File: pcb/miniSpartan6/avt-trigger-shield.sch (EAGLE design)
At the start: 20 parts

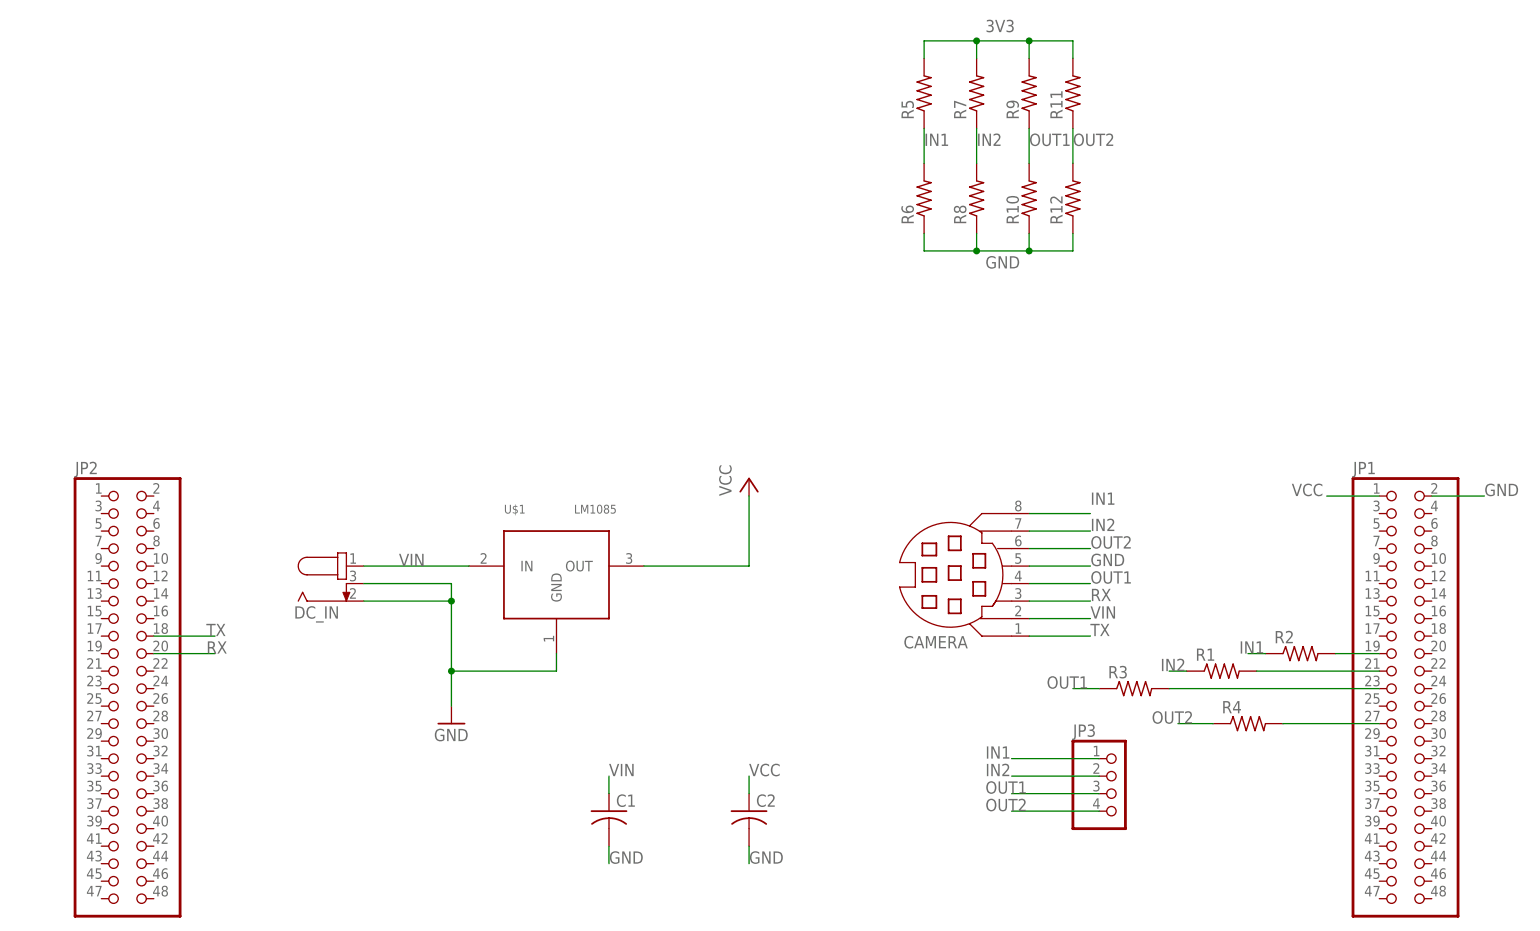
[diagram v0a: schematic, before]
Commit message: finished avt trigger board
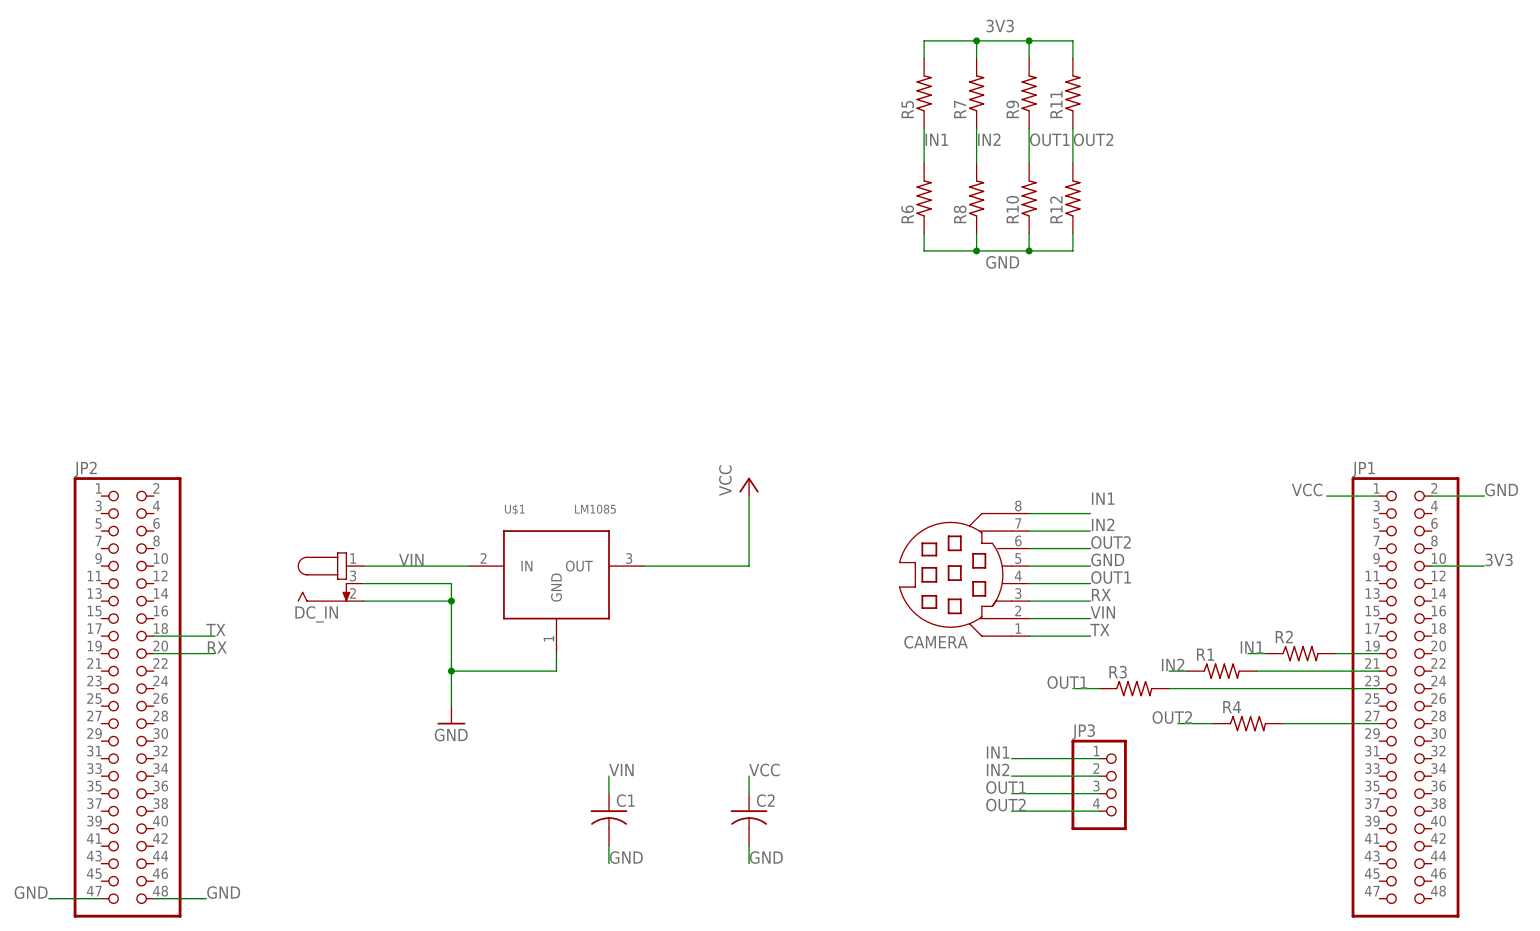
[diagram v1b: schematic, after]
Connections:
- net 3V3: now also JP1.10
- net GND: now also JP2.47, JP2.48
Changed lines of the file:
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@@
 <wire x1="142.24" y1="115.57" x2="142.24" y2="118.11" width="0.1524" layer="91"/>
+</segment>
+<segment>
+<pinref part="JP2" gate="A" pin="47"/>
+<wire x1="1.27" y1="21.59" x2="-6.35" y2="21.59" width="0.1524" layer="91"/>
+<label x="-11.43" y="21.59" size="1.778" layer="95"/>
+</segment>
+<segment>
+<pinref part="JP2" gate="A" pin="48"/>
+<wire x1="8.89" y1="21.59" x2="16.51" y2="21.59" width="0.1524" layer="91"/>
+<label x="16.51" y="21.59" size="1.778" layer="95"/>
 </segment>
 </net>
@@
 <label x="129.54" y="147.32" size="1.778" layer="95"/>
 </segment>
+<segment>
+<pinref part="JP1" gate="A" pin="10"/>
+<wire x1="194.31" y1="69.85" x2="201.93" y2="69.85" width="0.1524" layer="91"/>
+<label x="201.93" y="69.85" size="1.778" layer="95"/>
+</segment>
 </net>

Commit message: fixed pin assignments
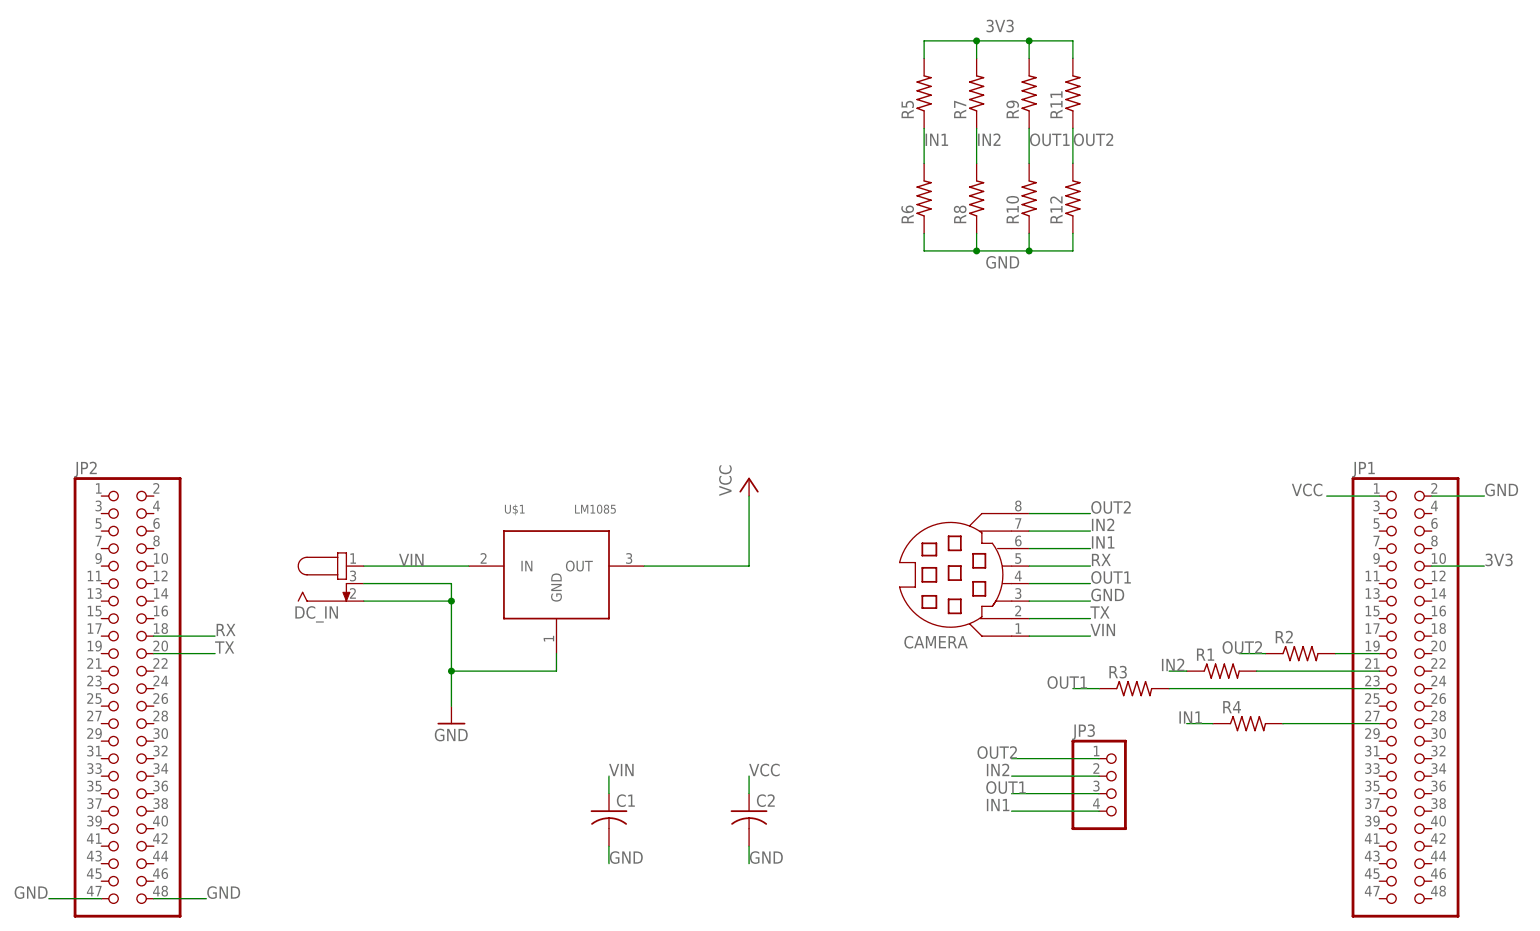
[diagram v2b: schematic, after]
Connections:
- net GND: now also CAMERA.3; no longer CAMERA.5
- net IN1: now also CAMERA.6, JP3.4, R4.1; no longer CAMERA.8, JP3.1, R2.1
- net OUT2: now also CAMERA.8, JP3.1, R2.1; no longer CAMERA.6, JP3.4, R4.1
- net RX: now also CAMERA.5, JP2.18; no longer CAMERA.3, JP2.20
- net TX: now also CAMERA.2, JP2.20; no longer CAMERA.1, JP2.18
- net VIN: now also CAMERA.1; no longer CAMERA.2
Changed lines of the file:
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@@
 </segment>
 <segment>
-<pinref part="CAMERA" gate="G$1" pin="2"/>
-<wire x1="135.89" y1="62.23" x2="144.78" y2="62.23" width="0.1524" layer="91"/>
-<label x="144.78" y="62.23" size="1.778" layer="95"/>
+<pinref part="CAMERA" gate="G$1" pin="1"/>
+<wire x1="135.89" y1="59.69" x2="144.78" y2="59.69" width="0.1524" layer="91"/>
+<label x="144.78" y="59.69" size="1.778" layer="95"/>
 </segment>
 </net>
@@
 </segment>
 <segment>
-<pinref part="CAMERA" gate="G$1" pin="5"/>
-<wire x1="135.89" y1="69.85" x2="144.78" y2="69.85" width="0.1524" layer="91"/>
-<label x="144.78" y="69.85" size="1.778" layer="95"/>
-</segment>
-<segment>
 <pinref part="R6" gate="G$1" pin="1"/>
 <wire x1="120.65" y1="118.11" x2="120.65" y2="115.57" width="0.1524" layer="91"/>
@@
 <label x="16.51" y="21.59" size="1.778" layer="95"/>
 </segment>
+<segment>
+<pinref part="CAMERA" gate="G$1" pin="3"/>
+<wire x1="135.89" y1="64.77" x2="144.78" y2="64.77" width="0.1524" layer="91"/>
+<label x="144.78" y="64.77" size="1.778" layer="95"/>
+</segment>
 </net>
 <net name="VCC" class="0">
@@
 <net name="TX" class="0">
 <segment>
-<pinref part="JP2" gate="A" pin="18"/>
-<wire x1="8.89" y1="59.69" x2="17.78" y2="59.69" width="0.1524" layer="91"/>
-<label x="16.51" y="59.69" size="1.778" layer="95"/>
+<pinref part="CAMERA" gate="G$1" pin="2"/>
+<wire x1="135.89" y1="62.23" x2="144.78" y2="62.23" width="0.1524" layer="91"/>
+<label x="144.78" y="62.23" size="1.778" layer="95"/>
 </segment>
 <segment>
-<pinref part="CAMERA" gate="G$1" pin="1"/>
-<wire x1="135.89" y1="59.69" x2="144.78" y2="59.69" width="0.1524" layer="91"/>
-<label x="144.78" y="59.69" size="1.778" layer="95"/>
+<pinref part="JP2" gate="A" pin="20"/>
+<wire x1="8.89" y1="57.15" x2="17.78" y2="57.15" width="0.1524" layer="91"/>
+<label x="17.78" y="57.15" size="1.778" layer="95"/>
 </segment>
 </net>
 <net name="RX" class="0">
 <segment>
-<pinref part="JP2" gate="A" pin="20"/>
-<wire x1="8.89" y1="57.15" x2="17.78" y2="57.15" width="0.1524" layer="91"/>
-<label x="16.51" y="57.15" size="1.778" layer="95"/>
+<pinref part="CAMERA" gate="G$1" pin="5"/>
+<wire x1="135.89" y1="69.85" x2="144.78" y2="69.85" width="0.1524" layer="91"/>
+<label x="144.78" y="69.85" size="1.778" layer="95"/>
 </segment>
 <segment>
-<pinref part="CAMERA" gate="G$1" pin="3"/>
-<wire x1="135.89" y1="64.77" x2="144.78" y2="64.77" width="0.1524" layer="91"/>
-<label x="144.78" y="64.77" size="1.778" layer="95"/>
+<pinref part="JP2" gate="A" pin="18"/>
+<wire x1="8.89" y1="59.69" x2="17.78" y2="59.69" width="0.1524" layer="91"/>
+<label x="17.78" y="59.69" size="1.778" layer="95"/>
 </segment>
 </net>
 <net name="IN1" class="0">
-<segment>
-<pinref part="CAMERA" gate="G$1" pin="8"/>
-<wire x1="135.89" y1="77.47" x2="144.78" y2="77.47" width="0.1524" layer="91"/>
-<label x="144.78" y="78.74" size="1.778" layer="95"/>
-</segment>
-<segment>
-<pinref part="JP3" gate="A" pin="1"/>
-<wire x1="146.05" y1="41.91" x2="133.35" y2="41.91" width="0.1524" layer="91"/>
-<label x="129.54" y="41.91" size="1.778" layer="95"/>
-</segment>
-<segment>
-<pinref part="R2" gate="G$1" pin="1"/>
-<wire x1="170.18" y1="57.15" x2="167.64" y2="57.15" width="0.1524" layer="91"/>
-<label x="166.37" y="57.15" size="1.778" layer="95"/>
-</segment>
 <segment>
 <pinref part="R6" gate="G$1" pin="2"/>
@@
 <wire x1="120.65" y1="128.27" x2="120.65" y2="133.35" width="0.1524" layer="91"/>
 <label x="120.65" y="130.81" size="1.778" layer="95"/>
+</segment>
+<segment>
+<pinref part="CAMERA" gate="G$1" pin="6"/>
+<wire x1="135.89" y1="72.39" x2="144.78" y2="72.39" width="0.1524" layer="91"/>
+<label x="144.78" y="72.39" size="1.778" layer="95"/>
+</segment>
+<segment>
+<pinref part="R4" gate="G$1" pin="1"/>
+<wire x1="162.56" y1="46.99" x2="158.75" y2="46.99" width="0.1524" layer="91"/>
+<label x="157.48" y="46.99" size="1.778" layer="95"/>
+</segment>
+<segment>
+<pinref part="JP3" gate="A" pin="4"/>
+<wire x1="146.05" y1="34.29" x2="133.35" y2="34.29" width="0.1524" layer="91"/>
+<label x="129.54" y="34.29" size="1.778" layer="95"/>
 </segment>
 </net>
@@
 <net name="OUT2" class="0">
 <segment>
-<pinref part="CAMERA" gate="G$1" pin="6"/>
-<wire x1="135.89" y1="72.39" x2="144.78" y2="72.39" width="0.1524" layer="91"/>
-<label x="144.78" y="72.39" size="1.778" layer="95"/>
-</segment>
-<segment>
-<pinref part="JP3" gate="A" pin="4"/>
-<wire x1="146.05" y1="34.29" x2="133.35" y2="34.29" width="0.1524" layer="91"/>
-<label x="129.54" y="34.29" size="1.778" layer="95"/>
-</segment>
-<segment>
-<pinref part="R4" gate="G$1" pin="1"/>
-<wire x1="162.56" y1="46.99" x2="157.48" y2="46.99" width="0.1524" layer="91"/>
-<label x="153.67" y="46.99" size="1.778" layer="95"/>
-</segment>
-<segment>
 <pinref part="R12" gate="G$1" pin="2"/>
 <pinref part="R11" gate="G$1" pin="1"/>
@@
 <label x="142.24" y="130.81" size="1.778" layer="95"/>
 </segment>
+<segment>
+<pinref part="CAMERA" gate="G$1" pin="8"/>
+<wire x1="135.89" y1="77.47" x2="144.78" y2="77.47" width="0.1524" layer="91"/>
+<label x="144.78" y="77.47" size="1.778" layer="95"/>
+</segment>
+<segment>
+<pinref part="JP3" gate="A" pin="1"/>
+<wire x1="146.05" y1="41.91" x2="133.35" y2="41.91" width="0.1524" layer="91"/>
+<label x="128.27" y="41.91" size="1.778" layer="95"/>
+</segment>
+<segment>
+<pinref part="R2" gate="G$1" pin="1"/>
+<wire x1="170.18" y1="57.15" x2="166.37" y2="57.15" width="0.1524" layer="91"/>
+<label x="163.83" y="57.15" size="1.778" layer="95"/>
+</segment>
 </net>
